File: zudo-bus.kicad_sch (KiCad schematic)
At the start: 56 parts, among them P1 WJ500V-5.08-2P-14-00A, P2 WJ500V-5.08-2P-14-00A, U10 2541WR-2X08P, U11 2541WR-2X08P, U12 1217754-1, U13 1217754-1, U14 1217754-1, U15 1217754-1, U2 2541WR-2X08P, U3 YLED0603YG, U4 NCD1608A1, U5 2541WR-2X08P, U6 2541WR-2X08P, U7 2541WR-2X08P, U8 2541WR-2X08P, U9 2541WR-2X08P

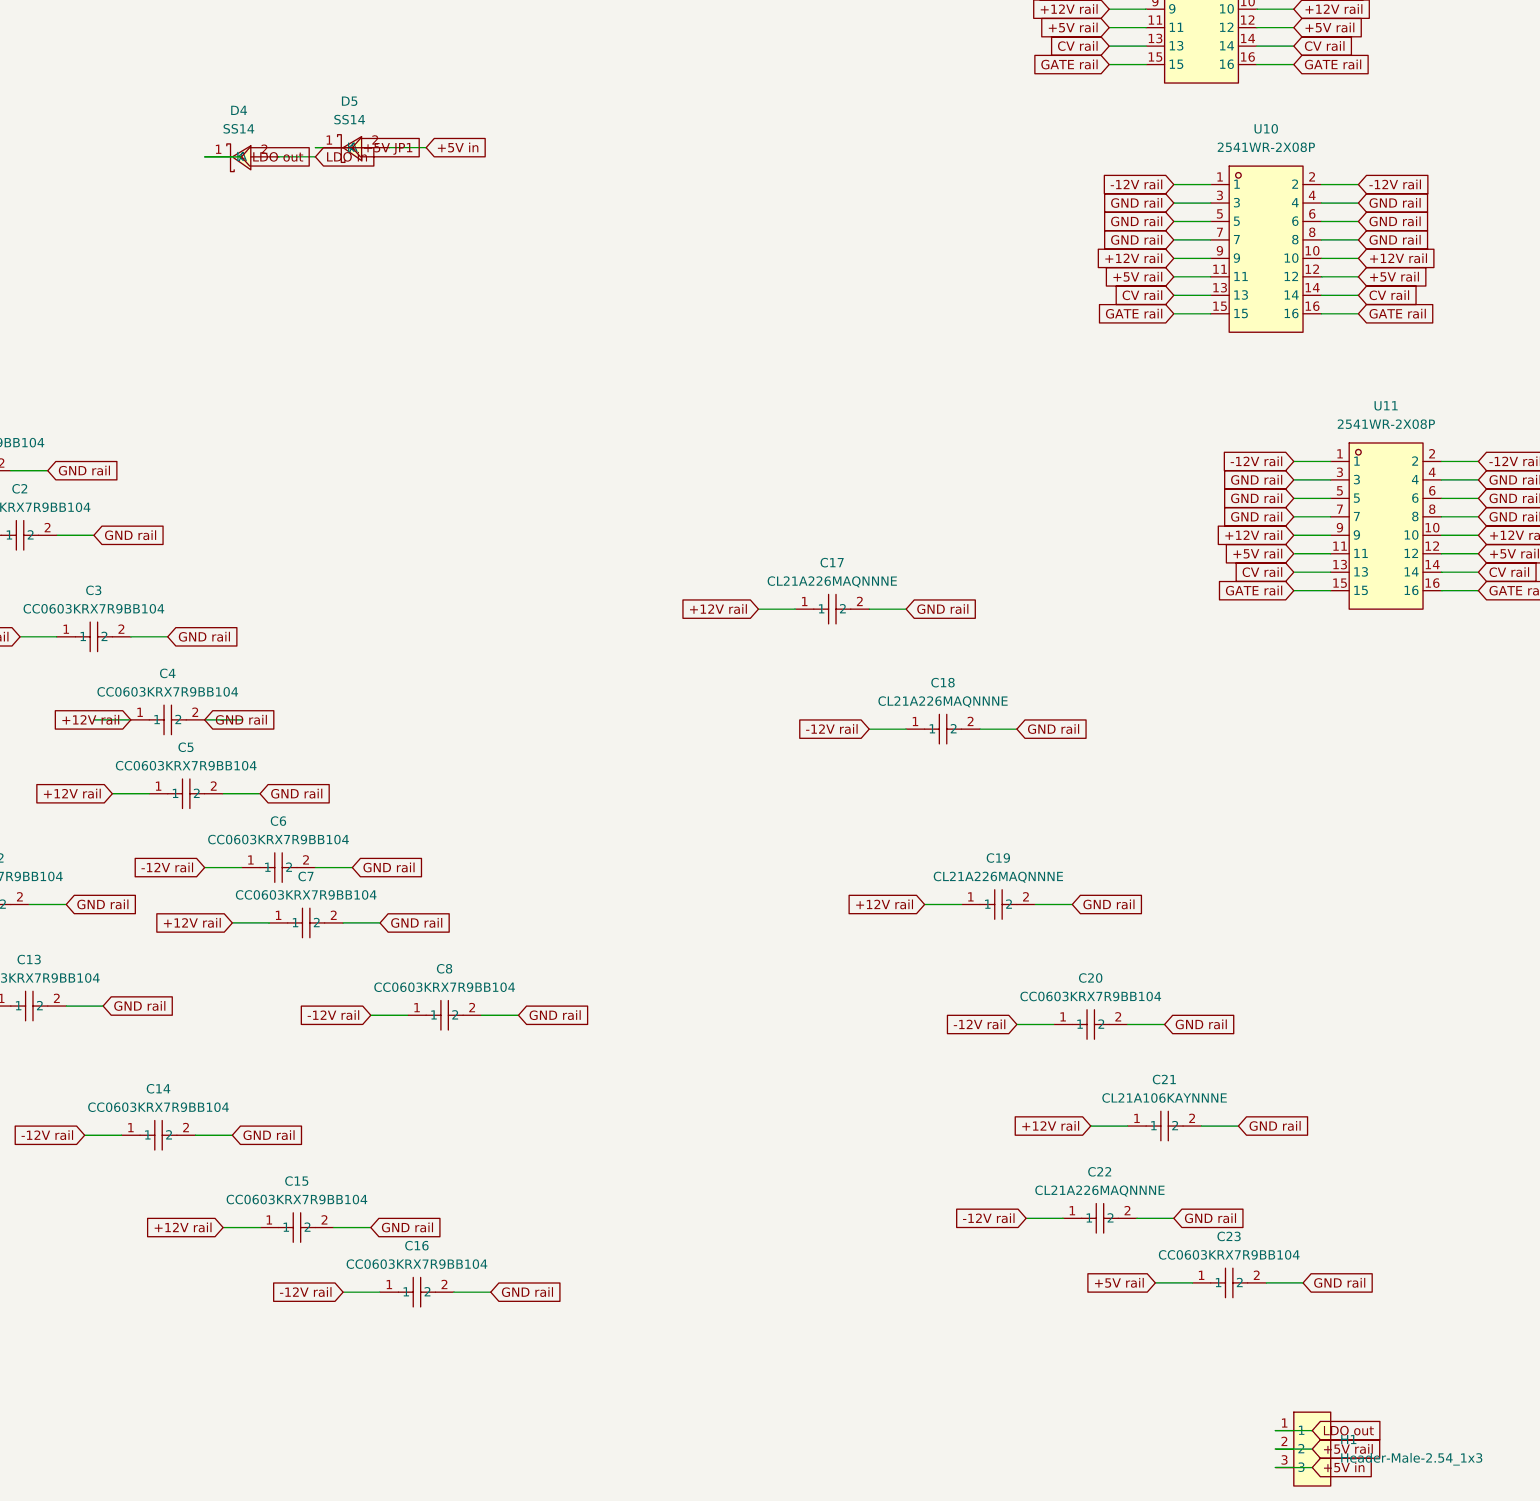
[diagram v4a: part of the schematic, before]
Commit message: Fix overlapping labels on H1 jumper and D4/D5 Schottky diodes
Flip label direction for components where labels overlapped:

H1 (3-pin jumper):
- LDO out, +5V rail, +5V in labels now point left instead of right
- Wires adjusted accordingly

D4/D5 (SS14 Schottky diodes):
- LDO out (D4 left pin) now points left
- +5V JP1 (D5 left pin) now points left
- Spreads labels out to avoid overlap in center

Remaining overlap issues (FASTON terminals, screw terminals) may need
manual adjustment in KiCad.

Co-Authored-By: Claude Opus 4.5 <noreply@anthropic.com>
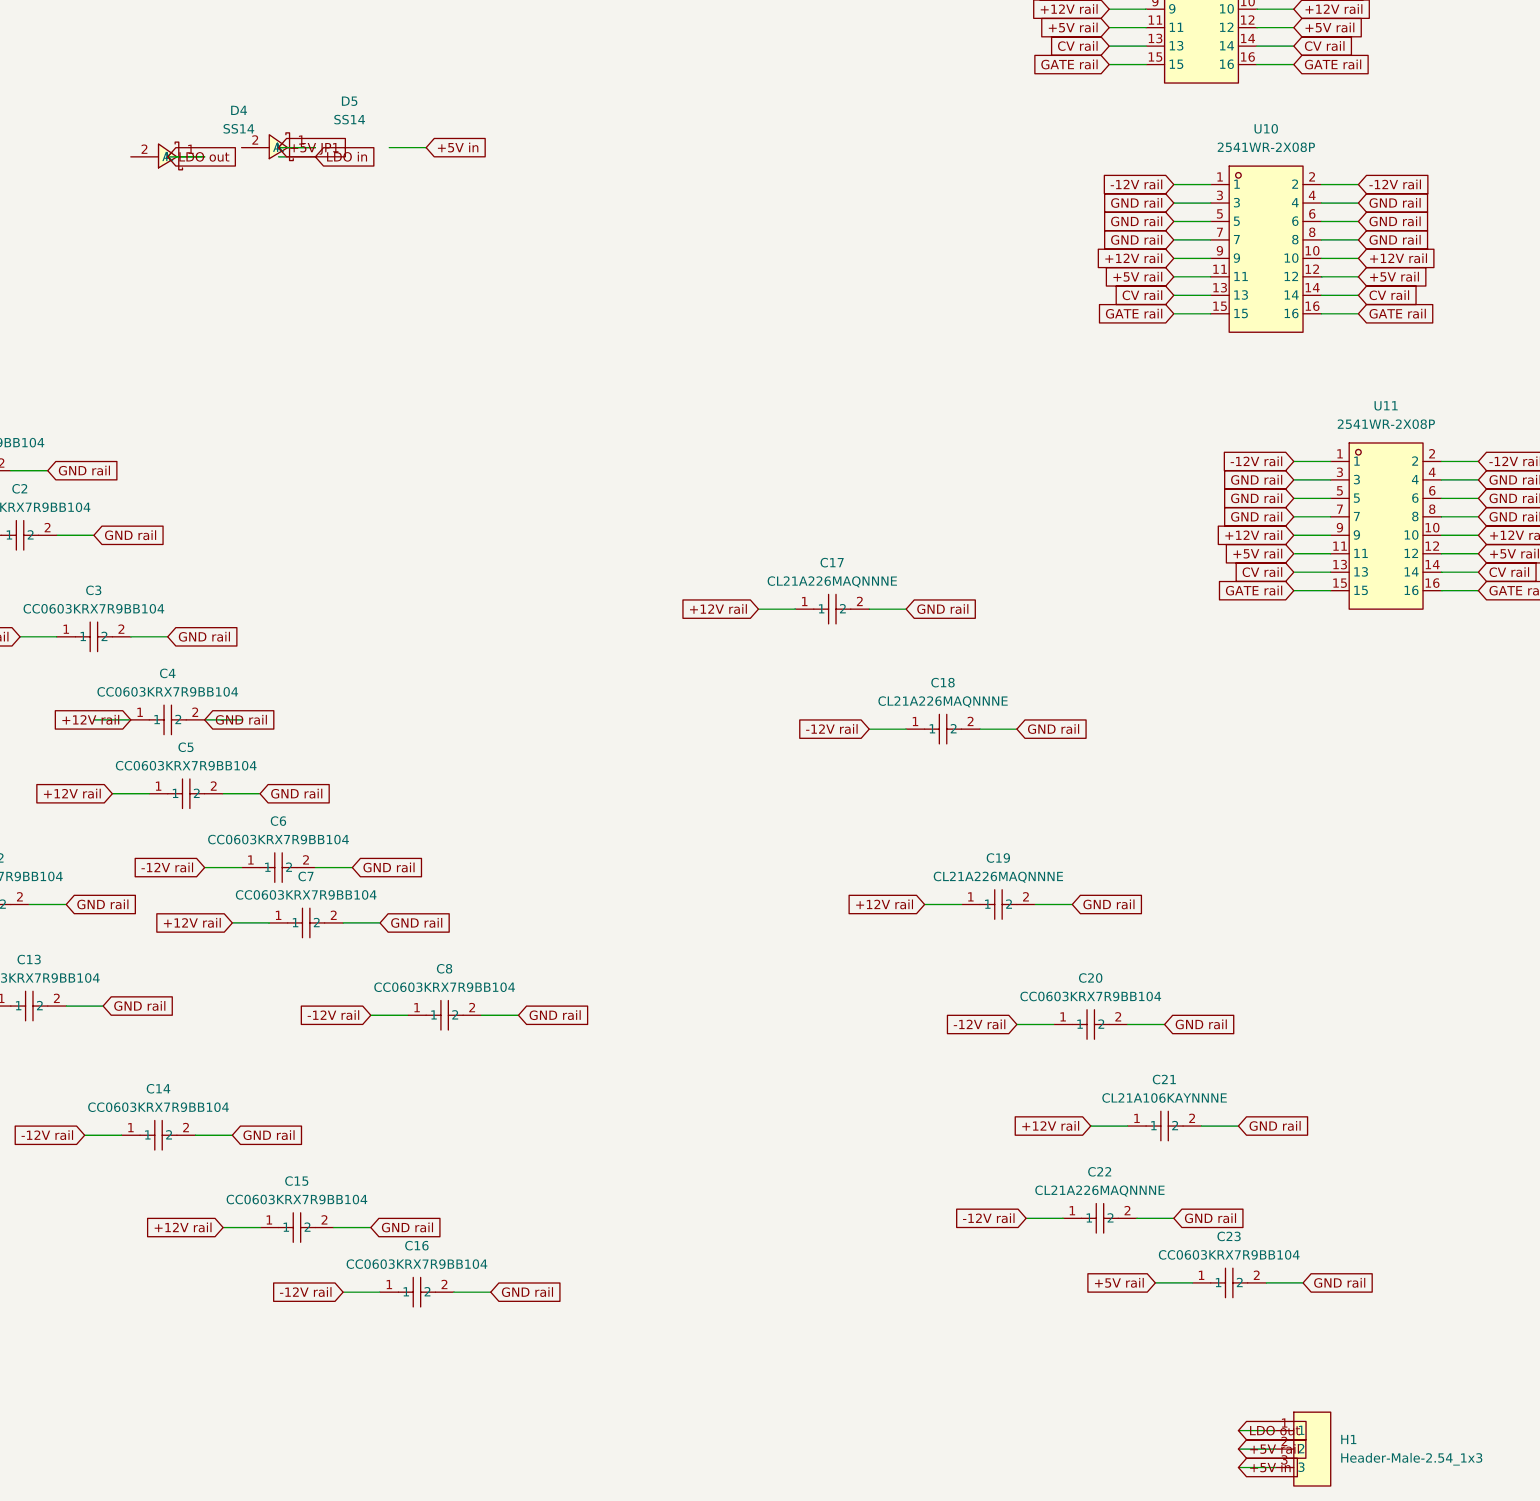
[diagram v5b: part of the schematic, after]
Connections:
- net +12V in: no longer D5.2 (A)
- net GND rail: no longer D4.2 (A)
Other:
- moved on the sheet: D4, D5
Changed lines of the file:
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@@
 	(symbol
 		(lib_id "zudo-bus-new-protection:SS14")
-		(at 125.73 175.26 0)
+		(at 115.57 175.26 180)
 		(unit 1)
 		(exclude_from_sim no)
@@
 		)
 		(property "Description" ""
-			(at 125.73 175.26 0)
+			(at 115.57 175.26 180)
 			(effects
 				(font
@@
 	(symbol
 		(lib_id "zudo-bus-new-protection:SS14")
-		(at 110.49 176.53 0)
+		(at 100.33 176.53 180)
 		(unit 1)
 		(exclude_from_sim no)
@@
 		)
 		(property "Description" ""
-			(at 110.49 176.53 0)
+			(at 100.33 176.53 180)
 			(effects
 				(font
@@
 	(global_label "LDO out"
 		(shape input)
-		(at 110.49 176.53 0)
+		(at 100.33 176.53 180)
 		(effects
 			(font
@@
 		(uuid "p0000001-0001-0001-0001-000000000015")
 		(property "Intersheetrefs" "${INTERSHEET_REFS}"
-			(at 105.41 176.53 0)
+			(at 100.33 176.53 180)
 			(effects
 				(font
@@
 	(global_label "+5V JP1"
 		(shape input)
-		(at 125.73 175.26 0)
+		(at 115.57 175.26 180)
 		(effects
 			(font
@@
 		(uuid "p0000001-0001-0001-0001-000000000017")
 		(property "Intersheetrefs" "${INTERSHEET_REFS}"
-			(at 120.65 175.26 0)
+			(at 115.57 175.26 180)
 			(effects
 				(font
@@
 	(global_label "LDO out"
 		(shape input)
-		(at 257.81 351.79 0)
+		(at 247.65 351.79 180)
 		(effects
 			(font
@@
 		(uuid "p0000001-0001-0001-0001-000000000038")
 		(property "Intersheetrefs" "${INTERSHEET_REFS}"
-			(at 252.73 351.79 0)
+			(at 247.65 351.79 180)
 			(effects
 				(font
@@
 	(global_label "+5V rail"
 		(shape input)
-		(at 257.81 354.33 0)
+		(at 247.65 354.33 180)
 		(effects
 			(font
@@
 		(uuid "p0000001-0001-0001-0001-000000000039")
 		(property "Intersheetrefs" "${INTERSHEET_REFS}"
-			(at 252.73 354.33 0)
+			(at 247.65 354.33 180)
 			(effects
 				(font
@@
 	(global_label "+5V in"
 		(shape input)
-		(at 257.81 356.87 0)
+		(at 247.65 356.87 180)
 		(effects
 			(font
@@
 		(uuid "p0000001-0001-0001-0001-000000000040")
 		(property "Intersheetrefs" "${INTERSHEET_REFS}"
-			(at 252.73 356.87 0)
+			(at 247.65 356.87 180)
 			(effects
 				(font
@@
 	(wire
 		(pts
-			(xy 105.41 176.53) (xy 110.49 176.53)
+			(xy 105.41 176.53) (xy 100.33 176.53)
 		)
 		(stroke
@@
 	(wire
 		(pts
-			(xy 120.65 175.26) (xy 125.73 175.26)
+			(xy 120.65 175.26) (xy 115.57 175.26)
 		)
 		(stroke
@@
 	(wire
 		(pts
-			(xy 252.73 351.79) (xy 257.81 351.79)
+			(xy 252.73 351.79) (xy 247.65 351.79)
 		)
 		(stroke
@@
 	(wire
 		(pts
-			(xy 252.73 354.33) (xy 257.81 354.33)
+			(xy 252.73 354.33) (xy 247.65 354.33)
 		)
 		(stroke
@@
 	(wire
 		(pts
-			(xy 252.73 356.87) (xy 257.81 356.87)
+			(xy 252.73 356.87) (xy 247.65 356.87)
 		)
 		(stroke

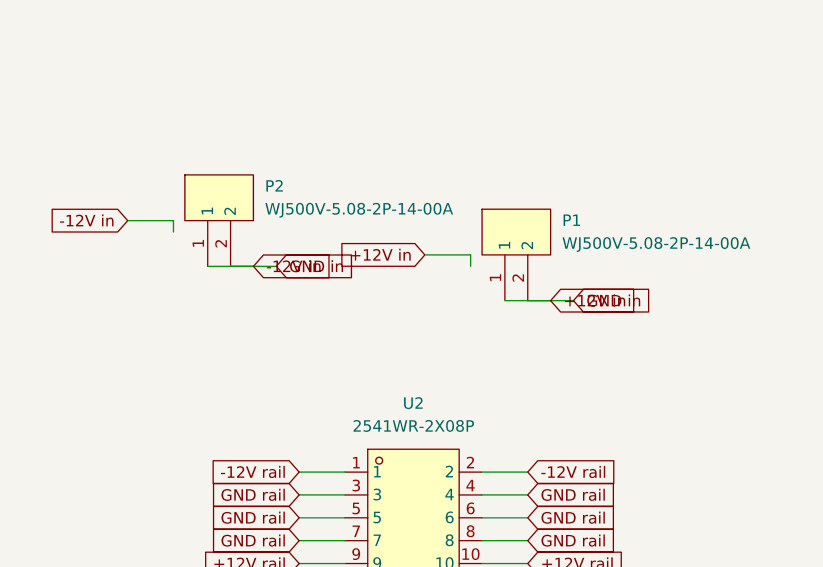
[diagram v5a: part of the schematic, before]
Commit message: Fix overlapping labels on P1/P2 screw terminals
Flip -12V in and +12V in labels to point left instead of right
to avoid overlap with adjacent GND in labels at same Y position.

- P2: -12V in at Y=53.34 flipped from rot=0 to rot=180
- P1: +12V in at Y=57.15 flipped from rot=0 to rot=180
- Updated corresponding wire endpoints

Co-Authored-By: Claude Opus 4.5 <noreply@anthropic.com>
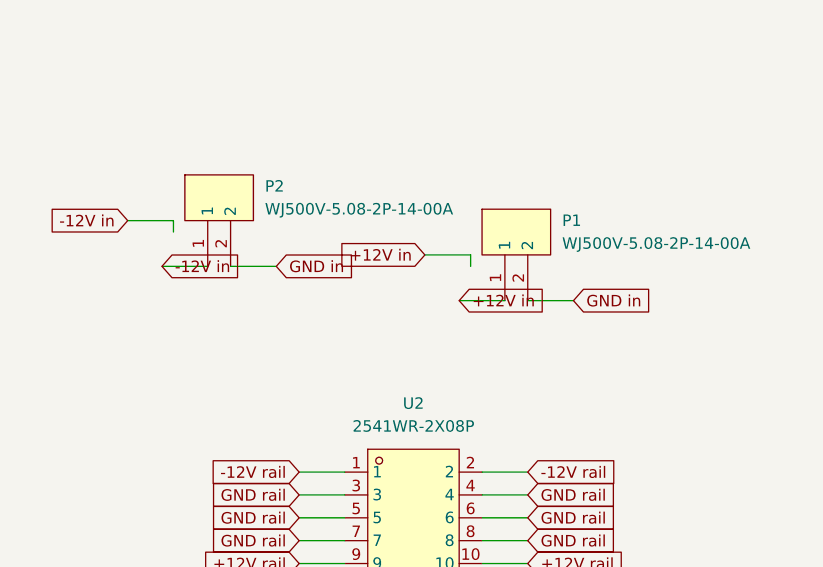
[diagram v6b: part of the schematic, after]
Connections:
- net +12V in: no longer D7.2 (A), D8.1 (C), F2.1, F3.1, F4.1, H1.3, P1.2, P2.1, P2.2, U13.1, U13.2, U14.1, U14.2, U15.1, U15.2
- new net +5V in: D7.2 (A), D8.1 (C), F2.1, F3.1, H1.3, P2.1, U13.1, U13.2, U14.1, U14.2
- new net GND in: F4.1, P1.2, P2.2, U15.1, U15.2
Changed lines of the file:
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@@
 	(global_label "+12V in"
 		(shape input)
-		(at 81.28 57.15 0)
+		(at 71.12 57.15 180)
 		(effects
 			(font
@@
 	(global_label "-12V in"
 		(shape input)
-		(at 48.26 53.34 0)
+		(at 38.1 53.34 180)
 		(effects
 			(font
@@
 	(wire
 		(pts
-			(xy 76.2 57.15) (xy 81.28 57.15)
+			(xy 76.2 57.15) (xy 71.12 57.15)
 		)
 		(stroke
@@
 	(wire
 		(pts
-			(xy 43.18 53.34) (xy 48.26 53.34)
-		)
-		(stroke
+			(xy 43.18 53.34) (xy 38.1 53.34)
+		)
+		(stroke

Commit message: Fix multiple overlapping label issues across schematic
Flip left-pin labels to point left (rot=180) to avoid overlap:

TVS Diodes:
- D1: GND rail label
- D2: +5V rail label
- D3: GND rail label

Protection Diodes (D6-D9):
- D6: +12V in label
- D7: GND rail label
- D8: +5V in label
- D9: LDO out label

LEDs:
- LED1: LED1_R1 label
- U3: GND rail label
- U4: GND rail label

Resistor:
- R1: LED1_R1 label

Schottky Diode:
- D5: +5V JP1 label (added wire)

Header:
- H1: +5V rail flipped to point right

FASTON Terminals:
- U12: +12V in label
- U13: -12V in label
- U14: +5V in label
- U15: GND in label

Co-Authored-By: Claude Opus 4.5 <noreply@anthropic.com>
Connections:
- net LDO out is gone; now on net GND rail: D4.1 (K), D9.1 (C), H1.1
- net +5V JP1: now also D5.2 (A)
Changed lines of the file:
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@@
 	(global_label "GND rail"
 		(shape input)
-		(at 91.44 -29.21 0)
+		(at 81.28 -29.21 180)
 		(effects
 			(font
@@
 	(global_label "+5V rail"
 		(shape input)
-		(at 116.84 -27.94 0)
+		(at 106.68 -27.94 180)
 		(effects
 			(font
@@
 	(global_label "GND rail"
 		(shape input)
-		(at 100.33 -13.97 0)
+		(at 90.17 -13.97 180)
 		(effects
 			(font
@@
 	(global_label "+12V in"
 		(shape input)
-		(at 59.69 3.81 0)
+		(at 49.53 3.81 180)
 		(effects
 			(font
@@
 	(global_label "GND rail"
 		(shape input)
-		(at 72.39 5.08 0)
+		(at 62.230000000000004 5.08 180)
 		(effects
 			(font
@@
 	(global_label "+5V in"
 		(shape input)
-		(at 87.63 5.08 0)
+		(at 77.47 5.08 180)
 		(effects
 			(font
@@
 	(global_label "LDO out"
 		(shape input)
-		(at 105.41 5.08 0)
+		(at 95.25 5.08 180)
 		(effects
 			(font
@@
 	(global_label "+5V JP1"
 		(shape input)
-		(at 115.57 175.26 180)
+		(at 110.49 175.26 180)
 		(effects
 			(font
@@
 	(global_label "LED1_R1"
 		(shape input)
-		(at 144.78 83.82 0)
+		(at 134.61999999999998 83.82 180)
 		(effects
 			(font
@@
 	(global_label "GND rail"
 		(shape input)
-		(at 144.78 106.68 0)
+		(at 134.61999999999998 106.68 180)
 		(effects
 			(font
@@
 	(global_label "GND rail"
 		(shape input)
-		(at 144.78 128.27 0)
+		(at 134.61999999999998 128.27 180)
 		(effects
 			(font
@@
 	(global_label "LED1_R1"
 		(shape input)
-		(at 78.74 140.97 0)
+		(at 68.58 140.97 180)
 		(effects
 			(font
@@
 	(global_label "GND in"
 		(shape input)
-		(at 229.87 19.05 0)
+		(at 219.70999999999998 19.05 180)
 		(effects
 			(font
@@
 	(global_label "+5V rail"
 		(shape input)
-		(at 247.65 354.33 180)
+		(at 257.81 354.33 0)
 		(effects
 			(font
@@
 	(wire
 		(pts
-			(xy 86.36 -29.21) (xy 91.44 -29.21)
-		)
-		(stroke
-			(width 0)
-			(type default)
-		)
-	)
-	(wire
-		(pts
-			(xy 111.76 -27.94) (xy 116.84 -27.94)
+			(xy 86.36 -29.21) (xy 81.28 -29.21)
+		)
+		(stroke
+			(width 0)
+			(type default)
+		)
+	)
+	(wire
+		(pts
+			(xy 111.76 -27.94) (xy 106.68 -27.94)
 		)
 		(stroke
@@
 	(wire
 		(pts
-			(xy 95.25 -13.97) (xy 100.33 -13.97)
-		)
-		(stroke
-			(width 0)
-			(type default)
-		)
-	)
-	(wire
-		(pts
-			(xy 54.61 3.81) (xy 59.69 3.81)
+			(xy 95.25 -13.97) (xy 90.17 -13.97)
+		)
+		(stroke
+			(width 0)
+			(type default)
+		)
+	)
+	(wire
+		(pts
+			(xy 54.61 3.81) (xy 49.53 3.81)
 		)
 		(stroke
@@
 	(wire
 		(pts
-			(xy 67.31 5.08) (xy 72.39 5.08)
+			(xy 67.31 5.08) (xy 62.230000000000004 5.08)
 		)
 		(stroke
@@
 	(wire
 		(pts
-			(xy 82.55 5.08) (xy 87.63 5.08)
+			(xy 82.55 5.08) (xy 77.47 5.08)
 		)
 		(stroke
@@
 	(wire
 		(pts
-			(xy 100.33 5.08) (xy 105.41 5.08)
+			(xy 100.33 5.08) (xy 95.25 5.08)
 		)
 		(stroke
@@
 	(wire
 		(pts
-			(xy 139.7 83.82) (xy 144.78 83.82)
+			(xy 139.7 83.82) (xy 134.61999999999998 83.82)
 		)
 		(stroke
@@
 	(wire
 		(pts
-			(xy 139.7 106.68) (xy 144.78 106.68)
+			(xy 139.7 106.68) (xy 134.61999999999998 106.68)
 		)
 		(stroke
@@
 	(wire
 		(pts
-			(xy 139.7 128.27) (xy 144.78 128.27)
+			(xy 139.7 128.27) (xy 134.61999999999998 128.27)
 		)
 		(stroke
@@
 	(wire
 		(pts
-			(xy 73.66 140.97) (xy 78.74 140.97)
+			(xy 73.66 140.97) (xy 68.58 140.97)
 		)
 		(stroke
@@
 	(wire
 		(pts
-			(xy 224.79 19.05) (xy 229.87 19.05)
+			(xy 224.79 19.05) (xy 219.70999999999998 19.05)
 		)
 		(stroke
@@
 	(wire
 		(pts
-			(xy 252.73 354.33) (xy 247.65 354.33)
+			(xy 252.73 354.33) (xy 257.81 354.33)
 		)
 		(stroke
@@
 	)
 	(embedded_fonts no)
+	(wire
+		(pts
+			(xy 115.57 175.26) (xy 110.49 175.26)
+		)
+		(stroke
+			(width 0)
+			(type default)
+		)
+	)
 )
